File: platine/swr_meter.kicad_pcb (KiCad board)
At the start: 2 copper layers, 23 parts, among them U1 CP0x0xx5425xNTR_Directional_C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, U2 LTC5530, U3 LM1117_SOT223, U4 STM32F030C8Tx, U5 STM32_mmvisual_JTAG, Y1 RESONATEUR

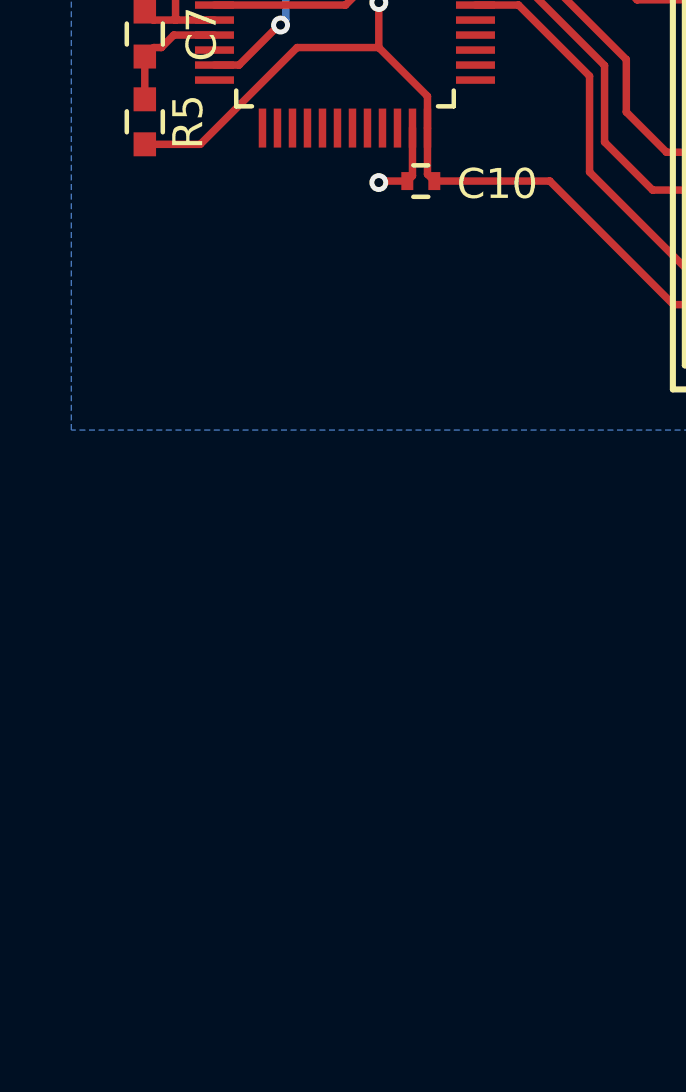
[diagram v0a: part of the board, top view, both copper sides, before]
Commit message: added one 7-segment display
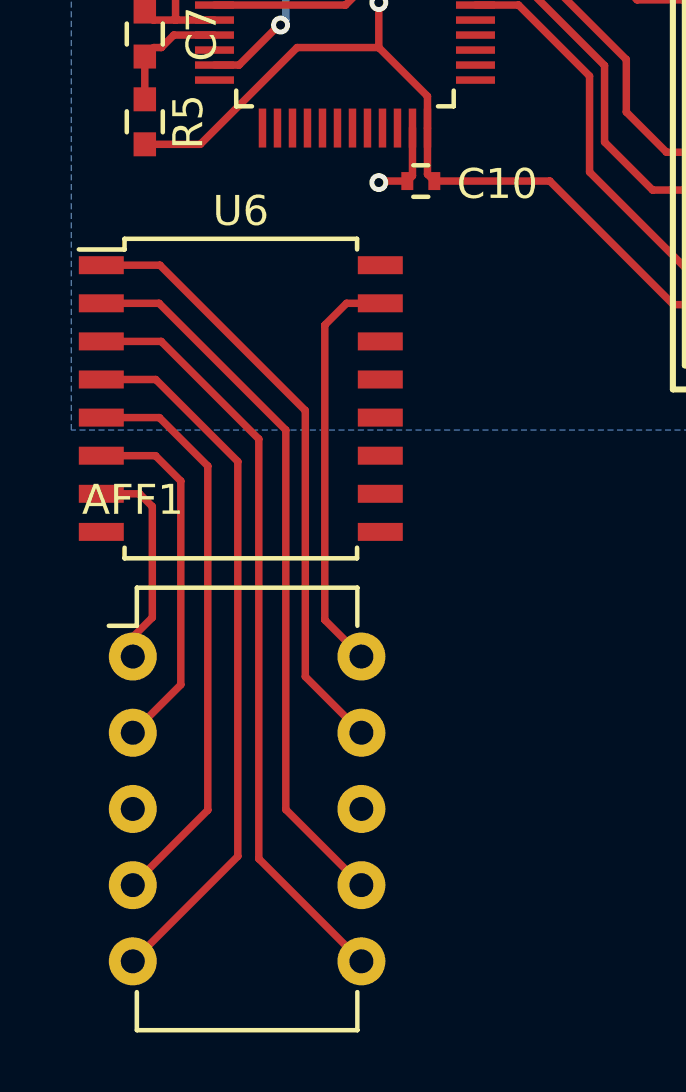
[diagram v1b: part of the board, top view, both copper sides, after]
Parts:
- added AFF1: 7SEGMENTS, Housings_DIP:DIP-10_W7.62mm, F.Cu at (151.1, 146.1)
- added U6: 74HC595, Housings_SOIC:SOIC-16_7.5x10.3mm_Pitch1.27mm, F.Cu at (154.7, 137.4)
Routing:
- net Net-(AFF1-Pad6): track 0.00 -> 25.4 mm
- net Net-(AFF1-Pad7): track 0.00 -> 24.1 mm
- net Net-(AFF1-Pad5): track 0.00 -> 23.8 mm
- net Net-(AFF1-Pad9): track 0.00 -> 20.3 mm
- net Net-(AFF1-Pad4): track 0.00 -> 19.2 mm
- net Net-(AFF1-Pad10): track 0.00 -> 13.7 mm
- net Net-(AFF1-Pad2): track 0.00 -> 12.1 mm
- net Net-(AFF1-Pad1): track 0.00 -> 7.15 mm

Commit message: work on 7-segment display
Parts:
- added AFF2: 7SEGMENTS, Housings_DIP:DIP-10_W7.62mm, F.Cu at (160.3, 148.9)
- added RP1: R_PACK4, Toni:R_array_4, F.Cu at (155.8, 144.5)
- added RP2: R_PACK4, Toni:R_array_4, F.Cu at (152.2, 144.5)
- added RP3: R_PACK4, Toni:R_array_4, F.Cu at (165.8, 144.5)
- added RP4: R_PACK4, Toni:R_array_4, F.Cu at (162.2, 144.5)
- added U7: 74HC595, Housings_SOIC:SOIC-16_3.9x9.9mm_Pitch1.27mm, F.Cu at (163.4, 136.7)
- U6: footprint Housings_SOIC:SOIC-16_7.5x10.3mm_Pitch1.27mm -> Housings_SOIC:SOIC-16_3.9x9.9mm_Pitch1.27mm
- moved AFF1 2.93 mm to (150.3, 148.9)
- moved U6 1.03 mm to (154.0, 136.7)
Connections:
- U6 pad 1: Net-(AFF1-Pad9) -> Net-(RP1-Pad2)
- U6 pad 15: Net-(AFF1-Pad10) -> Net-(RP1-Pad1)
- U6 pad 16: VCC -> +3V3
- U6 pad 2: Net-(AFF1-Pad7) -> Net-(RP1-Pad3)
- U6 pad 3: Net-(AFF1-Pad6) -> Net-(RP1-Pad4)
- U6 pad 4: Net-(AFF1-Pad5) -> Net-(RP2-Pad1)
- U6 pad 5: Net-(AFF1-Pad4) -> Net-(RP2-Pad2)
- U6 pad 6: Net-(AFF1-Pad2) -> Net-(RP2-Pad3)
- U6 pad 7: Net-(AFF1-Pad1) -> Net-(RP2-Pad4)
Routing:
- net +3V3: track 79.5 -> 149.9 mm, vias 4 -> 5
- net GND: track 115.0 -> 138.2 mm, vias 59 -> 61
- net Net-(U6-Pad9): track 0.00 -> 20.2 mm, vias 0 -> 2
- net Net-(AFF2-Pad6): track 0.00 -> 15.1 mm
- net Net-(AFF2-Pad5): track 0.00 -> 15.0 mm
- net Net-(RP3-Pad2): track 0.00 -> 14.4 mm
- net Net-(RP1-Pad2): track 0.00 -> 14.2 mm
- net Net-(AFF1-Pad9): track 20.3 -> 6.80 mm
- net Net-(RP3-Pad3): track 0.00 -> 12.9 mm
- net Net-(RP1-Pad3): track 0.00 -> 12.4 mm
- net Net-(AFF2-Pad7): track 0.00 -> 12.2 mm
- net Net-(AFF2-Pad4): track 0.00 -> 12.1 mm
- net Net-(RP1-Pad1): track 0.00 -> 12.0 mm
- net Net-(RP3-Pad1): track 0.00 -> 12.0 mm
- net Net-(AFF1-Pad7): track 24.1 -> 12.2 mm
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- added copper zone on B.Cu, net +3V3

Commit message: schematic complete, pcb complete, drc ok
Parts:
- added C11: 100nF, Resistors_SMD:R_0402, F.Cu at (164.4, 130.2)
- added C12: 100nF, Resistors_SMD:R_0402, F.Cu at (154.6, 130.6)
- added P1: Oled, Pin_Headers:Pin_Header_Straight_1x04, F.Cu at (165.4, 164.8)
- added P2: Vin, Pin_Headers:Pin_Header_Straight_1x02, F.Cu at (170.2, 119.8)
- Y1: value RESONATEUR -> 8 MHz
- moved C2 3.55 mm to (171.3, 116.8)
- moved U3 2.79 mm to (171.2, 111.2)
- moved C3 0.70 mm to (166.5, 113.7)
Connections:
- U4 pad 18: Net-(U4-Pad18) -> /spi_cs
- U4 pad 19: Net-(U4-Pad19) -> /shift_en
- U4 pad 21: Net-(U4-Pad21) -> /oled_scl
- U4 pad 22: Net-(U4-Pad22) -> /oled_sda
- U4 pad 39: Net-(U4-Pad39) -> /spi_sck
- U4 pad 41: Net-(U4-Pad41) -> /spi_mosi
- U4 pad 42: Net-(U4-Pad42) -> /shift_clear
- U6 pad 10: Net-(U6-Pad10) -> /shift_clear
- U6 pad 11: Net-(U6-Pad11) -> /spi_sck
- U6 pad 12: Net-(U6-Pad12) -> /spi_cs
- U6 pad 13: Net-(U6-Pad13) -> /shift_en
- U6 pad 14: Net-(U6-Pad14) -> /spi_mosi
- U7 pad 10: Net-(U7-Pad10) -> /shift_clear
- U7 pad 11: Net-(U7-Pad11) -> /spi_sck
- U7 pad 12: Net-(U7-Pad12) -> /spi_cs
- U7 pad 13: Net-(U7-Pad13) -> /shift_en
- Y1 pad 1: Net-(U4-Pad3) -> Net-(U4-Pad5)
- Y1 pad 3: Net-(U4-Pad4) -> Net-(U4-Pad6)
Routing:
- net /oled_sda: track 0.00 -> 78.6 mm, vias 0 -> 4
- net /oled_scl: track 0.00 -> 75.6 mm, vias 0 -> 2
- net /spi_sck: track 0.00 -> 50.6 mm, vias 0 -> 3
- net /shift_clear: track 0.00 -> 39.0 mm, vias 0 -> 7
- net /spi_mosi: track 0.00 -> 23.6 mm, vias 0 -> 4
- net GND: track 138.2 -> 160.4 mm, vias 61 -> 63
- net /spi_cs: track 0.00 -> 19.4 mm, vias 0 -> 5
- net +3V3: track 149.9 -> 168.8 mm
- net /shift_en: track 0.00 -> 17.6 mm, vias 0 -> 4
- net Net-(U4-Pad5): track 0.00 -> 4.82 mm
- net Net-(U4-Pad3): track 3.92 -> 0.00 mm
- net Net-(U4-Pad6): track 0.00 -> 3.49 mm
- net Net-(U4-Pad4): track 2.92 -> 0.00 mm
- net Net-(C2-Pad1): track 3.60 -> 5.97 mm
- net Net-(U6-Pad9): track 20.2 -> 19.4 mm

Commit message: i2c pullups added; outline added
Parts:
- added R6: 3,3k, Resistors_SMD:R_0603, F.Cu at (172.3, 146.0)
- added R7: 3,3k, Resistors_SMD:R_0603, F.Cu at (172.3, 147.7)
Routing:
- net +3V3: track 168.8 -> 174.3 mm, vias 5 -> 6
- net /oled_sda: track 78.6 -> 83.2 mm
- net /oled_scl: track 75.6 -> 76.4 mm
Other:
- board outline added: 26.8 x 77.8 mm
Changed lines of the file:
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@@
 (kicad_pcb (version 4) (host pcbnew 4.0.2-1.fc23-product)
   (general
-    (links 119)
+    (links 123)
     (no_connects 0)
-    (area 135.549499 89.5 188.300501 166.775001)
+    (area 0 0 0 0)
     (thickness 1.6)
-    (drawings 0)
-    (tracks 708)
+    (drawings 5)
+    (tracks 722)
     (zones 0)
-    (modules 35)
+    (modules 37)
     (nets 89)
   )
@@
     )
   )
+  (module Resistors_SMD:R_0603 (layer F.Cu)
+    (at 172.26 145.97 180)
+    (descr "Resistor SMD 0603, reflow soldering, Vishay (see dcrcw.pdf)")
+    (tags "resistor 0603")
+    (attr smd)
+    (fp_text reference R6 (at 0.11 1.72 180) (layer F.SilkS)
+      (effects (font (size 1 1) (thickness 0.15)))
+    )
+    (fp_text value 3,3k (at -0.28 3 180) (layer F.Fab)
+      (effects (font (size 1 1) (thickness 0.15)))
+    )
+    (fp_line (start -1.3 -0.8) (end 1.3 -0.8) (layer F.CrtYd) (width 0.05))
+    (fp_line (start -1.3 0.8) (end 1.3 0.8) (layer F.CrtYd) (width 0.05))
+    (fp_line (start -1.3 -0.8) (end -1.3 0.8) (layer F.CrtYd) (width 0.05))
+    (fp_line (start 1.3 -0.8) (end 1.3 0.8) (layer F.CrtYd) (width 0.05))
+    (fp_line (start 0.5 0.675) (end -0.5 0.675) (layer F.SilkS) (width 0.15))
+    (fp_line (start -0.5 -0.675) (end 0.5 -0.675) (layer F.SilkS) (width 0.15))
+    (pad 1 smd rect (at -0.75 0 180) (size 0.5 0.9) (layers F.Cu F.Paste F.Mask)
+      (net 38 +3V3))
+    (pad 2 smd rect (at 0.75 0 180) (size 0.5 0.9) (layers F.Cu F.Paste F.Mask)
+      (net 85 /oled_sda))
+    (model Resistors_SMD.3dshapes/R_0603.wrl
+      (at (xyz 0 0 0))
+      (scale (xyz 1 1 1))
+      (rotate (xyz 0 0 0))
+    )
+  )
+  (module Resistors_SMD:R_0603 (layer F.Cu)
+    (at 172.27 147.65 180)
+    (descr "Resistor SMD 0603, reflow soldering, Vishay (see dcrcw.pdf)")
+    (tags "resistor 0603")
+    (attr smd)
+    (fp_text reference R7 (at 0 -1.54 180) (layer F.SilkS)
+      (effects (font (size 1 1) (thickness 0.15)))
+    )
+    (fp_text value 3,3k (at -0.27 -2.86 180) (layer F.Fab)
+      (effects (font (size 1 1) (thickness 0.15)))
+    )
+    (fp_line (start -1.3 -0.8) (end 1.3 -0.8) (layer F.CrtYd) (width 0.05))
+    (fp_line (start -1.3 0.8) (end 1.3 0.8) (layer F.CrtYd) (width 0.05))
+    (fp_line (start -1.3 -0.8) (end -1.3 0.8) (layer F.CrtYd) (width 0.05))
+    (fp_line (start 1.3 -0.8) (end 1.3 0.8) (layer F.CrtYd) (width 0.05))
+    (fp_line (start 0.5 0.675) (end -0.5 0.675) (layer F.SilkS) (width 0.15))
+    (fp_line (start -0.5 -0.675) (end 0.5 -0.675) (layer F.SilkS) (width 0.15))
+    (pad 1 smd rect (at -0.75 0 180) (size 0.5 0.9) (layers F.Cu F.Paste F.Mask)
+      (net 38 +3V3))
+    (pad 2 smd rect (at 0.75 0 180) (size 0.5 0.9) (layers F.Cu F.Paste F.Mask)
+      (net 84 /oled_scl))
+    (model Resistors_SMD.3dshapes/R_0603.wrl
+      (at (xyz 0 0 0))
+      (scale (xyz 1 1 1))
+      (rotate (xyz 0 0 0))
+    )
+  )
+  (gr_line (start 148.5 166.75) (end 148.5 89) (angle 90) (layer Edge.Cuts) (width 0.15))
+  (gr_line (start 148.75 166.75) (end 148.5 166.75) (angle 90) (layer Edge.Cuts) (width 0.15))
+  (gr_line (start 175.25 166.75) (end 148.75 166.75) (angle 90) (layer Edge.Cuts) (width 0.15))
+  (gr_line (start 175.25 89) (end 175.25 166.75) (angle 90) (layer Edge.Cuts) (width 0.15))
+  (gr_line (start 148.5 89) (end 175.25 89) (angle 90) (layer Edge.Cuts) (width 0.15))
   (segment (start 158.999999 143.325001) (end 158.996001 143.328999) (width 0.152) (layer F.Cu) (net 0))
   (segment (start 172.69 119.775) (end 172.69 117.19) (width 0.5) (layer F.Cu) (net 1))
@@
   (segment (start 160.555 96.945) (end 160.45682 97.04318) (width 0.23) (layer F.Cu) (net 37))
   (segment (start 160.45682 97.04318) (end 160.4 97.1) (width 0.23) (layer F.Cu) (net 37))
+  (segment (start 173.01 145.97) (end 173.01 145.04) (width 0.25) (layer F.Cu) (net 38))
+  (segment (start 172.97 145.08) (end 170.18 145.08) (width 0.25) (layer B.Cu) (net 38))
+  (segment (start 173.01 145.04) (end 172.97 145.08) (width 0.25) (layer B.Cu) (net 38))
+  (via (at 173.01 145.04) (size 0.63) (drill 0.3) (layers F.Cu B.Cu) (net 38))
+  (segment (start 173.01 145.97) (end 173.01 147.64) (width 0.25) (layer F.Cu) (net 38))
+  (segment (start 173.01 147.64) (end 173.02 147.65) (width 0.25) (layer F.Cu) (net 38))
   (segment (start 174.25 120.5) (end 174.25 115.675) (width 0.5) (layer B.Cu) (net 38))
   (segment (start 173.75 139) (end 174.25 138.5) (width 0.5) (layer B.Cu) (net 38))
@@
   (segment (start 167.97 153.98) (end 168 153.95) (width 0.5) (layer B.Cu) (net 38))
   (segment (start 168 153.95) (end 169.65 153.95) (width 0.5) (layer B.Cu) (net 38))
-  (segment (start 170.18 153.42) (end 170.18 139) (width 0.5) (layer B.Cu) (net 38))
   (segment (start 169.65 153.95) (end 170.18 153.42) (width 0.5) (layer B.Cu) (net 38))
+  (segment (start 170.18 153.42) (end 170.18 145.08) (width 0.5) (layer B.Cu) (net 38))
+  (segment (start 170.18 145.08) (end 170.18 139) (width 0.5) (layer B.Cu) (net 38))
   (segment (start 158.25 123.25) (end 155.45 123.25) (width 0.25) (layer F.Cu) (net 38))
   (segment (start 154.825 120.925) (end 154.825 121.825) (width 0.25) (layer F.Cu) (net 38))
@@
   (segment (start 159.19 136.015) (end 159.275 136.1) (width 0.23) (layer F.Cu) (net 83))
   (segment (start 166.135 136.065) (end 166.15 136.065) (width 0.23) (layer F.Cu) (net 83))
+  (segment (start 171.52 147.65) (end 170.925 147.65) (width 0.25) (layer F.Cu) (net 84))
+  (segment (start 170.925 147.65) (end 170.775 147.8) (width 0.25) (layer F.Cu) (net 84))
   (segment (start 149.168838 131.918746) (end 149.168838 144.430891) (width 0.23) (layer F.Cu) (net 84))
   (segment (start 151.092594 129.99499) (end 149.168838 131.918746) (width 0.23) (layer F.Cu) (net 84))
@@
   (segment (start 160.32 164.85) (end 160.32 163.604) (width 0.23) (layer F.Cu) (net 84))
   (segment (start 160.32 163.604) (end 160.949 162.975) (width 0.23) (layer F.Cu) (net 84))
+  (segment (start 171.51 145.97) (end 170.39 145.97) (width 0.25) (layer F.Cu) (net 85))
+  (segment (start 168.675 145.665) (end 168.675 147.1) (width 0.25) (layer F.Cu) (net 85))
+  (segment (start 168.9 145.44) (end 168.675 145.665) (width 0.25) (layer F.Cu) (net 85))
+  (segment (start 169.86 145.44) (end 168.9 145.44) (width 0.25) (layer F.Cu) (net 85))
+  (segment (start 170.39 145.97) (end 169.86 145.44) (width 0.25) (layer F.Cu) (net 85))
+  (segment (start 170.35 148.35) (end 169.1 147.1) (width 0.23) (layer F.Cu) (net 85))
+  (segment (start 169.1 147.1) (end 168.675 147.1) (width 0.23) (layer F.Cu) (net 85))
+  (segment (start 170.35 161.775) (end 170.35 148.35) (width 0.23) (layer F.Cu) (net 85))
+  (segment (start 169.6 162.525) (end 170.35 161.775) (width 0.23) (layer F.Cu) (net 85))
+  (segment (start 158.859 162.525) (end 169.6 162.525) (width 0.23) (layer F.Cu) (net 85))
+  (segment (start 157.78 163.604) (end 158.859 162.525) (width 0.23) (layer F.Cu) (net 85))
+  (via (at 168.675 147.1) (size 0.63) (drill 0.3) (layers F.Cu B.Cu) (net 85))
   (segment (start 159.125 126.275) (end 159.8722 127.0222) (width 0.23) (layer F.Cu) (net 85))
   (segment (start 159.8722 127.0222) (end 159.8722 128.4337) (width 0.23) (layer F.Cu) (net 85))
@@
   (via (at 149.525 146.05) (size 0.63) (drill 0.3) (layers F.Cu B.Cu) (net 85))
   (segment (start 168.675 147.1) (end 150.575 147.1) (width 0.23) (layer B.Cu) (net 85))
-  (segment (start 170.35 148.35) (end 169.1 147.1) (width 0.23) (layer F.Cu) (net 85))
-  (segment (start 169.1 147.1) (end 168.675 147.1) (width 0.23) (layer F.Cu) (net 85))
-  (via (at 168.675 147.1) (size 0.63) (drill 0.3) (layers F.Cu B.Cu) (net 85))
-  (segment (start 170.35 161.775) (end 170.35 148.35) (width 0.23) (layer F.Cu) (net 85))
-  (segment (start 169.6 162.525) (end 170.35 161.775) (width 0.23) (layer F.Cu) (net 85))
-  (segment (start 158.859 162.525) (end 169.6 162.525) (width 0.23) (layer F.Cu) (net 85))
   (segment (start 157.78 164.85) (end 157.78 163.604) (width 0.23) (layer F.Cu) (net 85))
-  (segment (start 157.78 163.604) (end 158.859 162.525) (width 0.23) (layer F.Cu) (net 85))
   (segment (start 174.2 137.4) (end 172.629062 138.970938) (width 0.16) (layer F.Cu) (net 86))
   (segment (start 169.131221 138.970938) (end 168.685744 138.970938) (width 0.16) (layer F.Cu) (net 86))

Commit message: gerberfiles dazugefügt und auf der Platine einen kleinen Text geschrieben.
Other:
- board text added: "Antenne"
- board text added: "Sender"
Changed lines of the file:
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@@
-(kicad_pcb (version 4) (host pcbnew 4.0.2-1.fc23-product)
+(kicad_pcb (version 4) (host pcbnew "(2016-03-18 BZR 6629)-product")
   (general
     (links 123)
     (no_connects 0)
-    (area 0 0 0 0)
+    (area 135.549499 88.924999 188.300501 166.825001)
     (thickness 1.6)
-    (drawings 5)
+    (drawings 7)
     (tracks 722)
     (zones 0)
@@
     (visible_elements FFFFFF7F)
     (pcbplotparams
-      (layerselection 0x00030_80000001)
-      (usegerberextensions false)
+      (layerselection 0x010f0_ffffffff)
+      (usegerberextensions true)
       (excludeedgelayer true)
       (linewidth 0.100000)
@@
       (hpglpenspeed 20)
       (hpglpendiameter 15)
-      (hpglpenoverlay 2)
       (psnegative false)
       (psa4output false)
       (plotreference true)
-      (plotvalue true)
+      (plotvalue false)
       (plotinvisibletext false)
       (padsonsilk false)
-      (subtractmaskfromsilk false)
+      (subtractmaskfromsilk true)
       (outputformat 1)
       (mirror false)
-      (drillshape 1)
+      (drillshape 0)
       (scaleselection 1)
-      (outputdirectory ""))
+      (outputdirectory gerber/))
   )
   (net 0 "")
@@
     )
   )
+  (gr_text Antenne (at 154 104) (layer F.SilkS)
+    (effects (font (size 1.5 1.5) (thickness 0.3)))
+  )
+  (gr_text Sender (at 170.5 104) (layer F.SilkS)
+    (effects (font (size 1.5 1.5) (thickness 0.3)))
+  )
   (gr_line (start 148.5 166.75) (end 148.5 89) (angle 90) (layer Edge.Cuts) (width 0.15))

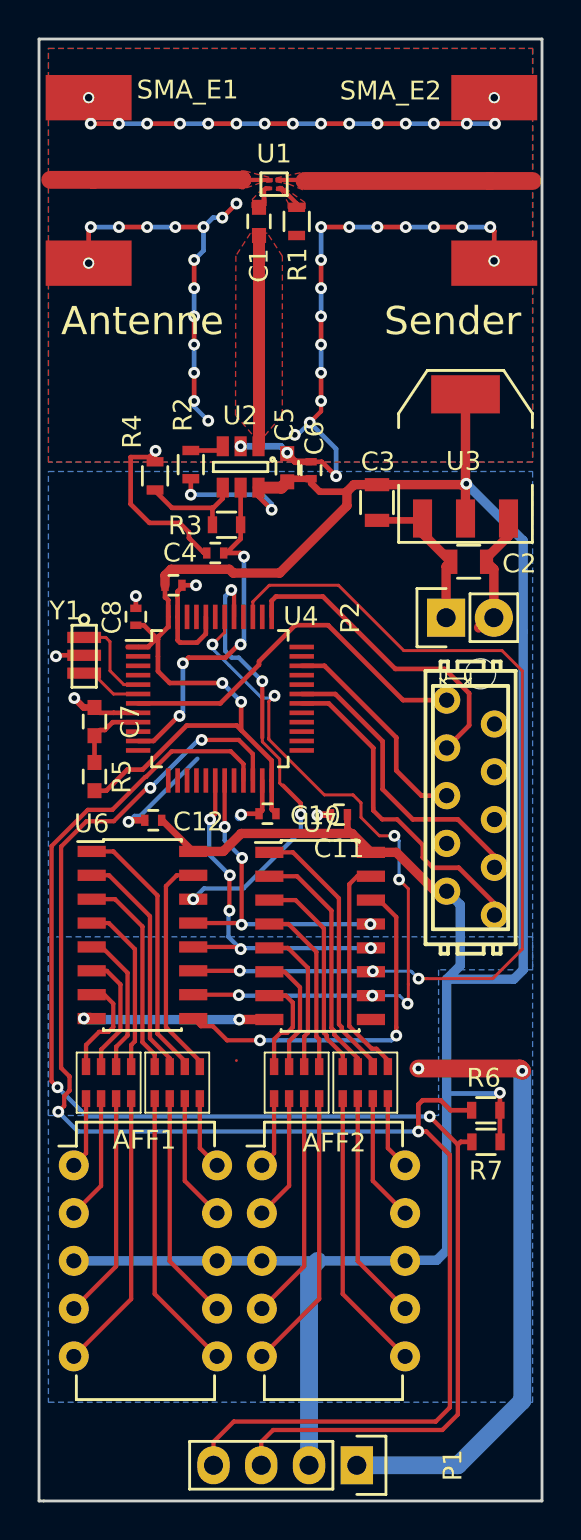
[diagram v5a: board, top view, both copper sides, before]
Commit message: changed minimal isolation distance to 160um
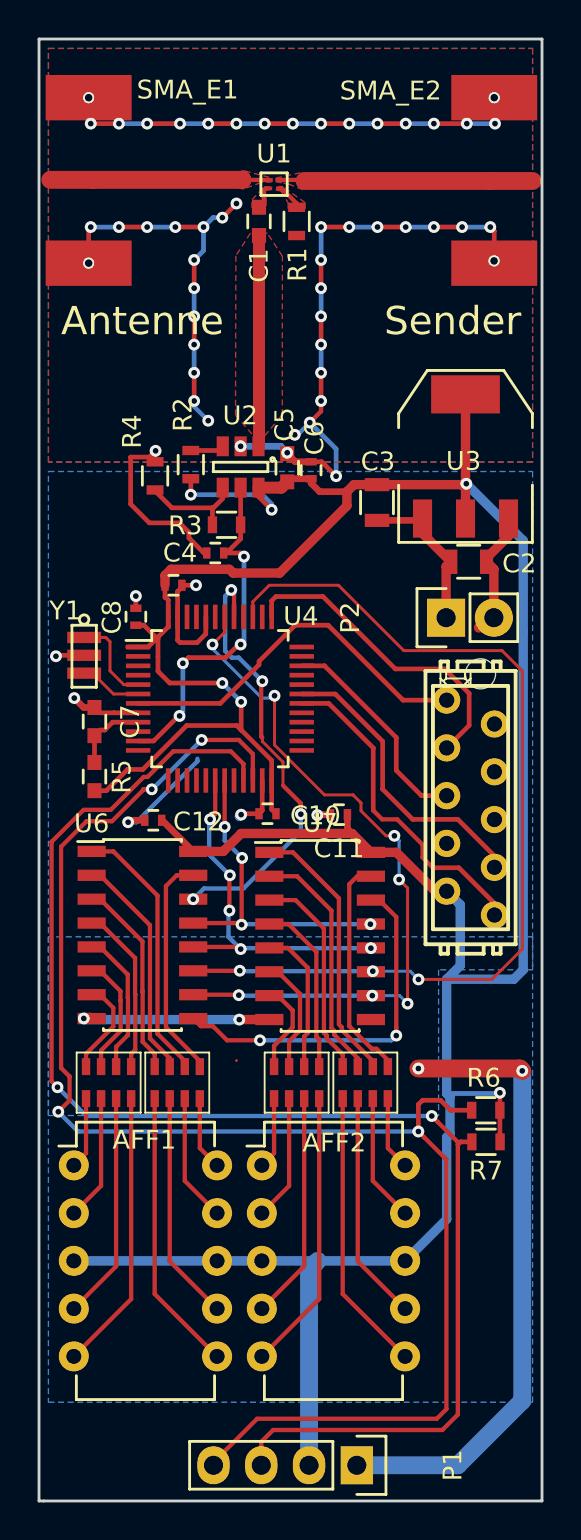
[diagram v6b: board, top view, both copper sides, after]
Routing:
- net /oled_sda: track 83.2 -> 82.1 mm
- net +3V3: track 174.3 -> 173.5 mm
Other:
- net class Default: clearance 0.15 -> 0.16
- rule trace_clearance: 0.15 -> 0.16
